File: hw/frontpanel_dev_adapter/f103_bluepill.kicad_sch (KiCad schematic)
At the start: 47 parts, among them J501 Conn_01x20, J502 Conn_01x20, J503 SWD, J504 STX-3501-3N_(TTL-232R-xV-AJ), J505 Conn_01x03, Q501 AO3401A, SW501 SKHUxxE010, U501 STM32F103CBTx, U502 W25Q128JVSIQ, U503 AT24C256C-SSHL, U504 DS3231M, Y501 16MHz

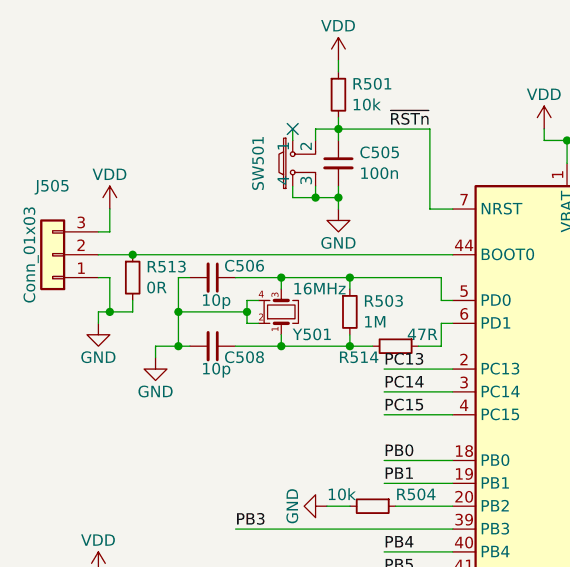
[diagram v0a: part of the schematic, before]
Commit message: hw: long-standing uncommitted stuff; mostly auto-updates (v7) fw: remove L052 tree (CMSIS & std-HAL shouldn't be committed and it was the wrong device name anyway)
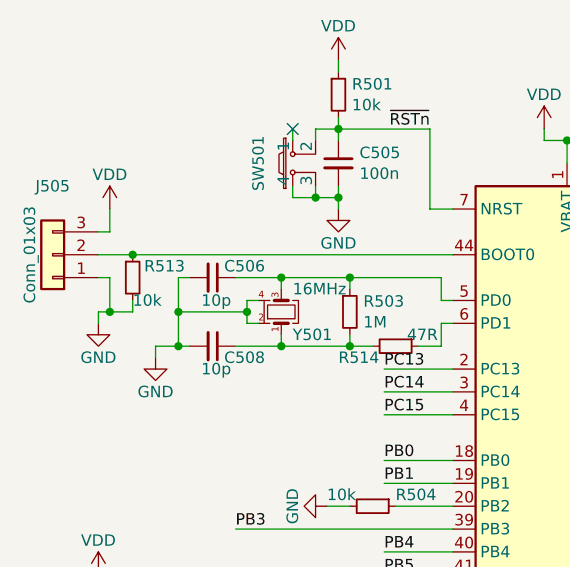
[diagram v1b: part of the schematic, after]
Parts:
- R513: value 0R -> 10k; LCSC C17168 -> C25744
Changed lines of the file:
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@@
   (junction (at 46.99 26.67) (diameter 0) (color 0 0 0 0)
   )
-  (junction (at 219.71 99.06) (diameter 0) (color 0 0 0 0)
-  )
   (junction (at 24.13 40.64) (diameter 0) (color 0 0 0 0)
   )
+  (junction (at 219.71 99.06) (diameter 0) (color 0 0 0 0)
+  )
   (junction (at 74.93 109.22) (diameter 0) (color 0 0 0 0)
   )
@@
     (stroke (width 0) (type default) (color 0 0 0 0))
   )
-  (wire (pts (xy 24.13 40.64) (xy 59.69 40.64))
-    (stroke (width 0) (type default) (color 0 0 0 0))
-  )
   (wire (pts (xy 210.82 87.63) (xy 210.82 90.17))
     (stroke (width 0) (type default) (color 0 0 0 0))
@@
     (stroke (width 0) (type default) (color 0 0 0 0))
   )
+  (wire (pts (xy 24.13 40.64) (xy 59.69 40.64))
+    (stroke (width 0) (type default) (color 0 0 0 0))
+  )
   (wire (pts (xy 267.97 30.48) (xy 250.19 30.48))
     (stroke (width 0) (type default) (color 0 0 0 0))
@@
     (pin "1")
   )
-  (symbol (lib_id "Device:R_Small") (at 24.13 43.18 0) (unit 1)
-    (in_bom yes) (on_board yes)
-    (property "Reference" "R513" (id 0) (at 25.6286 42.0116 0)
-      (effects (font (size 1.27 1.27)) (justify left))
-    )
-    (property "Value" "0R" (id 1) (at 25.6286 44.323 0)
-      (effects (font (size 1.27 1.27)) (justify left))
-    )
-    (property "Footprint" "Resistor_SMD:R_0402_1005Metric" (id 2) (at 24.13 43.18 0)
-      (effects (font (size 1.27 1.27)) hide)
-    )
-    (property "Datasheet" "~" (id 3) (at 24.13 43.18 0)
-      (effects (font (size 1.27 1.27)) hide)
-    )
-    (property "LCSC" "C17168" (id 4) (at 24.13 43.18 0)
-      (effects (font (size 1.27 1.27)) hide)
-    )
-    (pin "1")
-    (pin "2")
-  )
   (symbol (lib_id "power:GND") (at 45.72 68.58 270) (unit 1)
     (in_bom yes) (on_board yes)
@@
     (pin "1")
   )
+  (symbol (lib_id "Device:R_Small") (at 24.13 43.18 0) (unit 1)
+    (in_bom yes) (on_board yes)
+    (property "Reference" "R513" (id 0) (at 25.4 41.91 0)
+      (effects (font (size 1.27 1.27)) (justify left))
+    )
+    (property "Value" "10k" (id 1) (at 24.13 45.72 0)
+      (effects (font (size 1.27 1.27)) (justify left))
+    )
+    (property "Footprint" "Resistor_SMD:R_0402_1005Metric" (id 2) (at 24.13 43.18 0)
+      (effects (font (size 1.27 1.27)) hide)
+    )
+    (property "Datasheet" "~" (id 3) (at 24.13 43.18 0)
+      (effects (font (size 1.27 1.27)) hide)
+    )
+    (property "LCSC" "C25744" (id 4) (at 24.13 43.18 90)
+      (effects (font (size 1.27 1.27)) hide)
+    )
+    (pin "1")
+    (pin "2")
+  )
 )

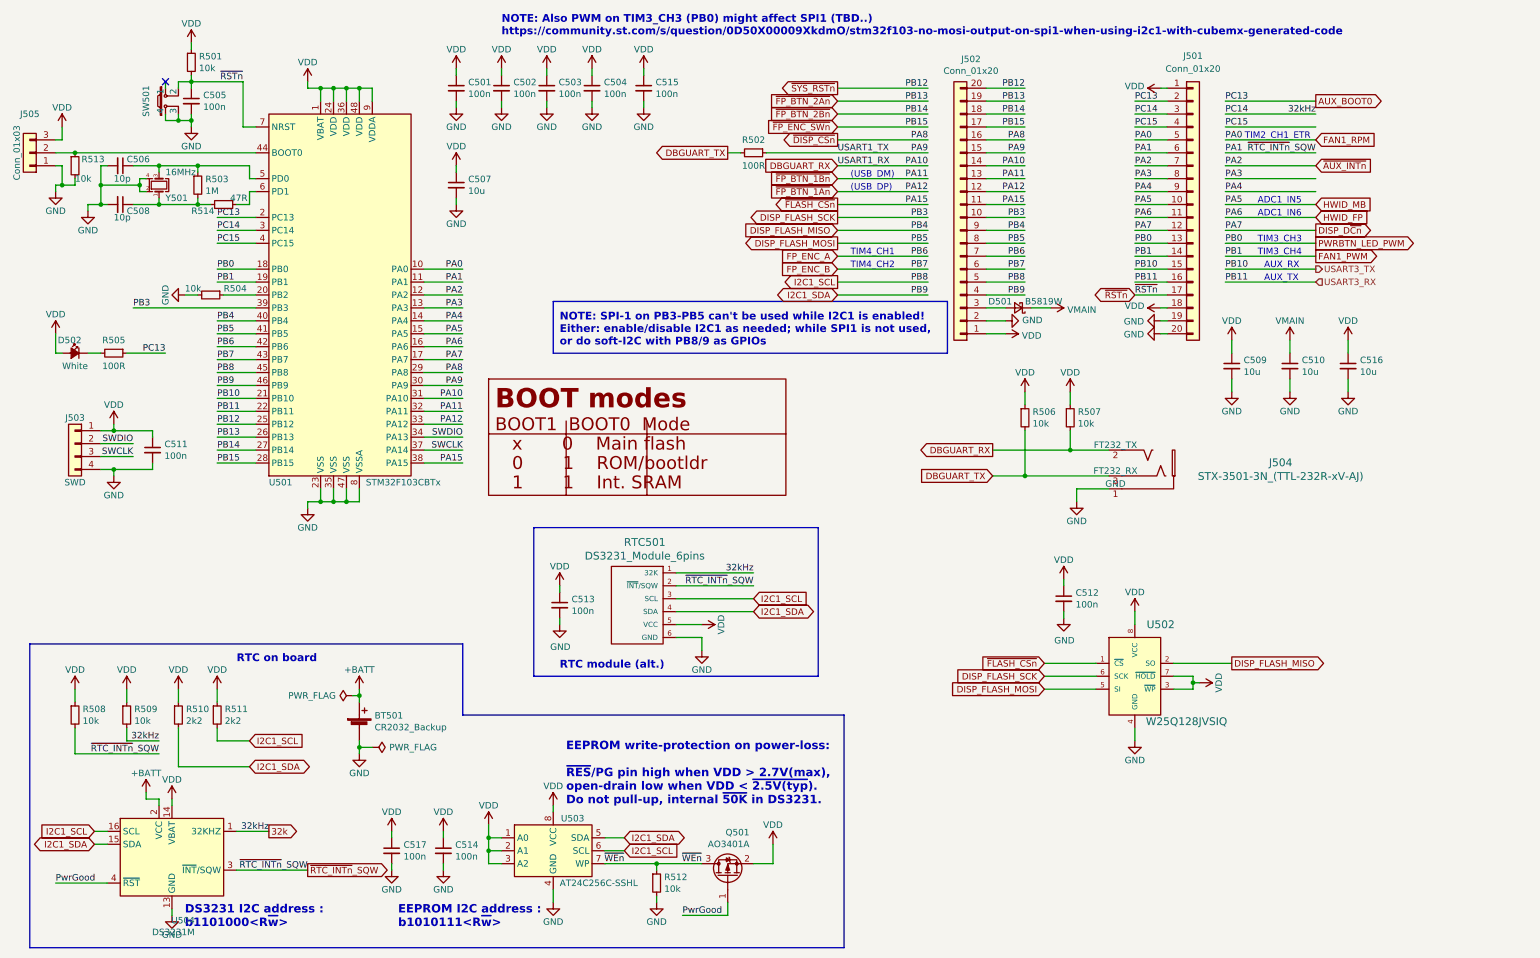
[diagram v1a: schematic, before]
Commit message: Various boards & schematics (auto-)updated to Kicad-v8
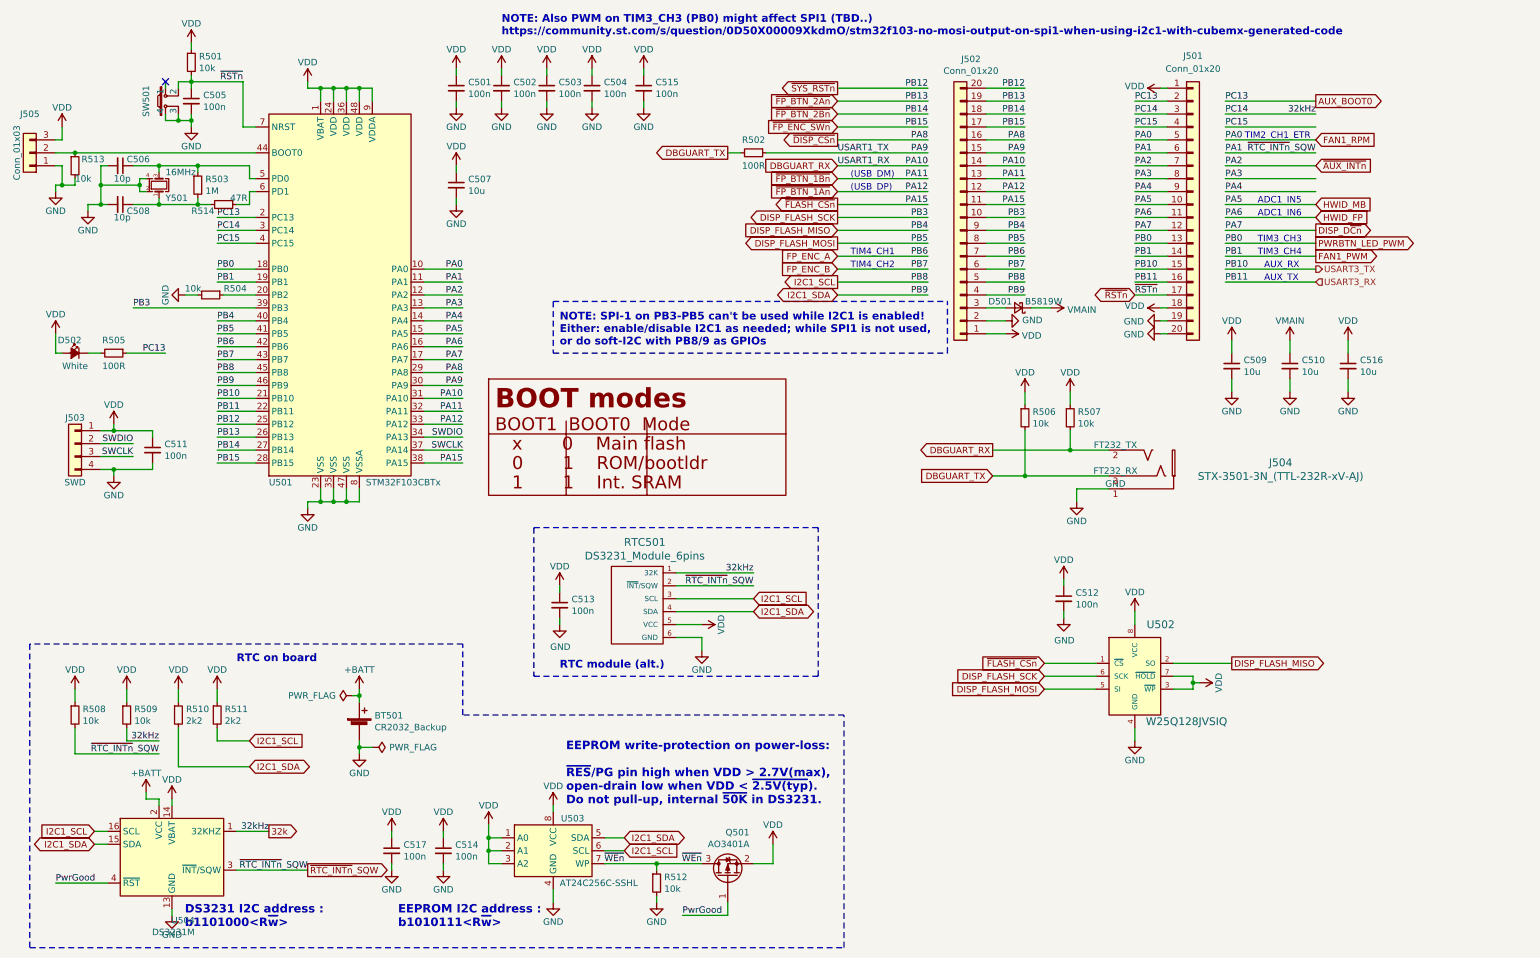
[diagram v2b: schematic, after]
